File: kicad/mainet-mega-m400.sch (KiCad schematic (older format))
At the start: 4 parts, among them J40 Screw_Terminal_01x04, J64 Screw_Terminal_01x09, J65 Screw_Terminal_01x17, J66 Screw_Terminal_01x02

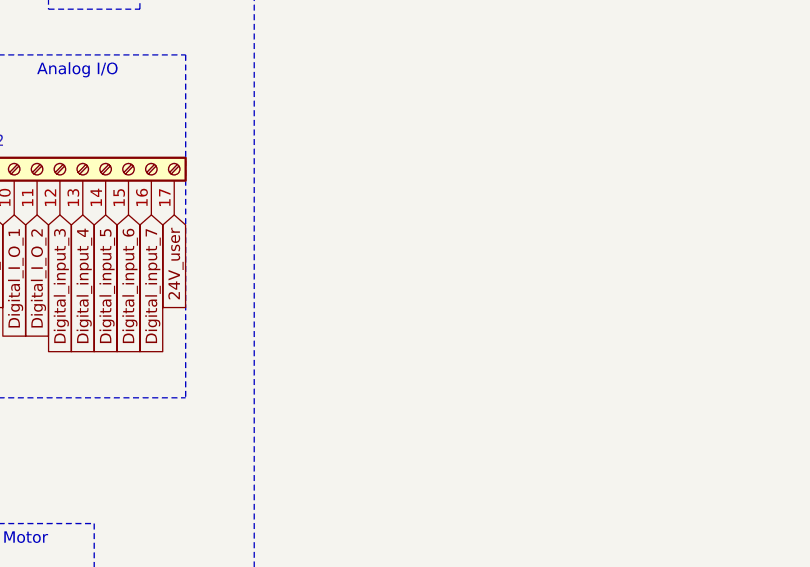
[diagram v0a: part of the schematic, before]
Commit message: KICAD: Actualizar esquemáticos
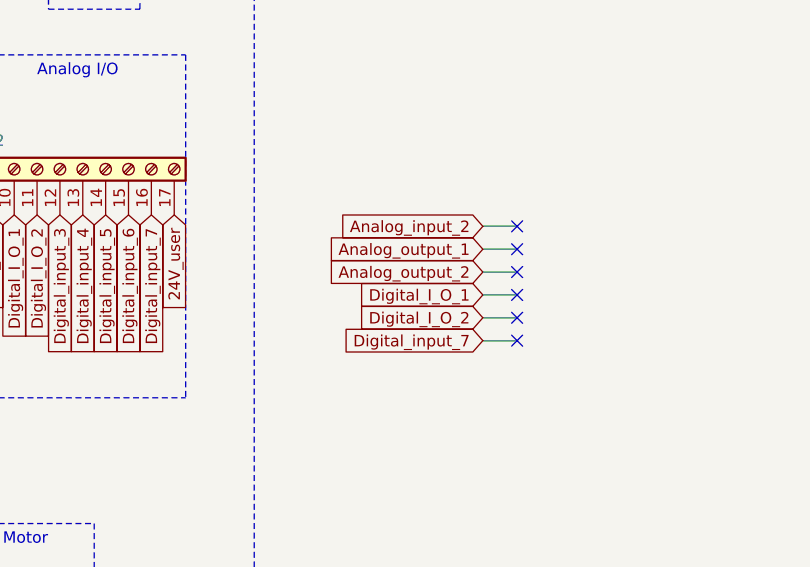
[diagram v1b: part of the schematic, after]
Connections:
- no-connect marks 6 -> 12
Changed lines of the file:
@@
 encoding utf-8
 Sheet 20 21
-Title "Mainet-mega -- "
-Date "2021-04-06"
+Title "Mainet-mega -- Diagrama de Conexiones del M400"
+Date "2021-04-07"
 Rev "1.0"
 Comp "Tovenca"
@@
 W
 NoConn ~ 7450 4450
+NoConn ~ 5800 5150
+NoConn ~ 5800 4950
+NoConn ~ 5800 5050
+NoConn ~ 5800 4850
+NoConn ~ 5800 4750
+NoConn ~ 5800 4650
+Text GLabel 5650 4650 0    50   Input ~ 0
+Analog_input_2
+Wire Wire Line
+	5650 4650 5800 4650
+Text GLabel 5650 4750 0    50   Input ~ 0
+Analog_output_1
+Text GLabel 5650 4850 0    50   Input ~ 0
+Analog_output_2
+Text GLabel 5650 4950 0    50   Input ~ 0
+Digital_I_O_1
+Text GLabel 5650 5050 0    50   Input ~ 0
+Digital_I_O_2
+Text GLabel 5650 5150 0    50   Input ~ 0
+Digital_input_7
+Wire Wire Line
+	5650 4750 5800 4750
+Wire Wire Line
+	5650 4850 5800 4850
+Wire Wire Line
+	5650 4950 5800 4950
+Wire Wire Line
+	5650 5050 5800 5050
+Wire Wire Line
+	5650 5150 5800 5150
 $EndSCHEMATC

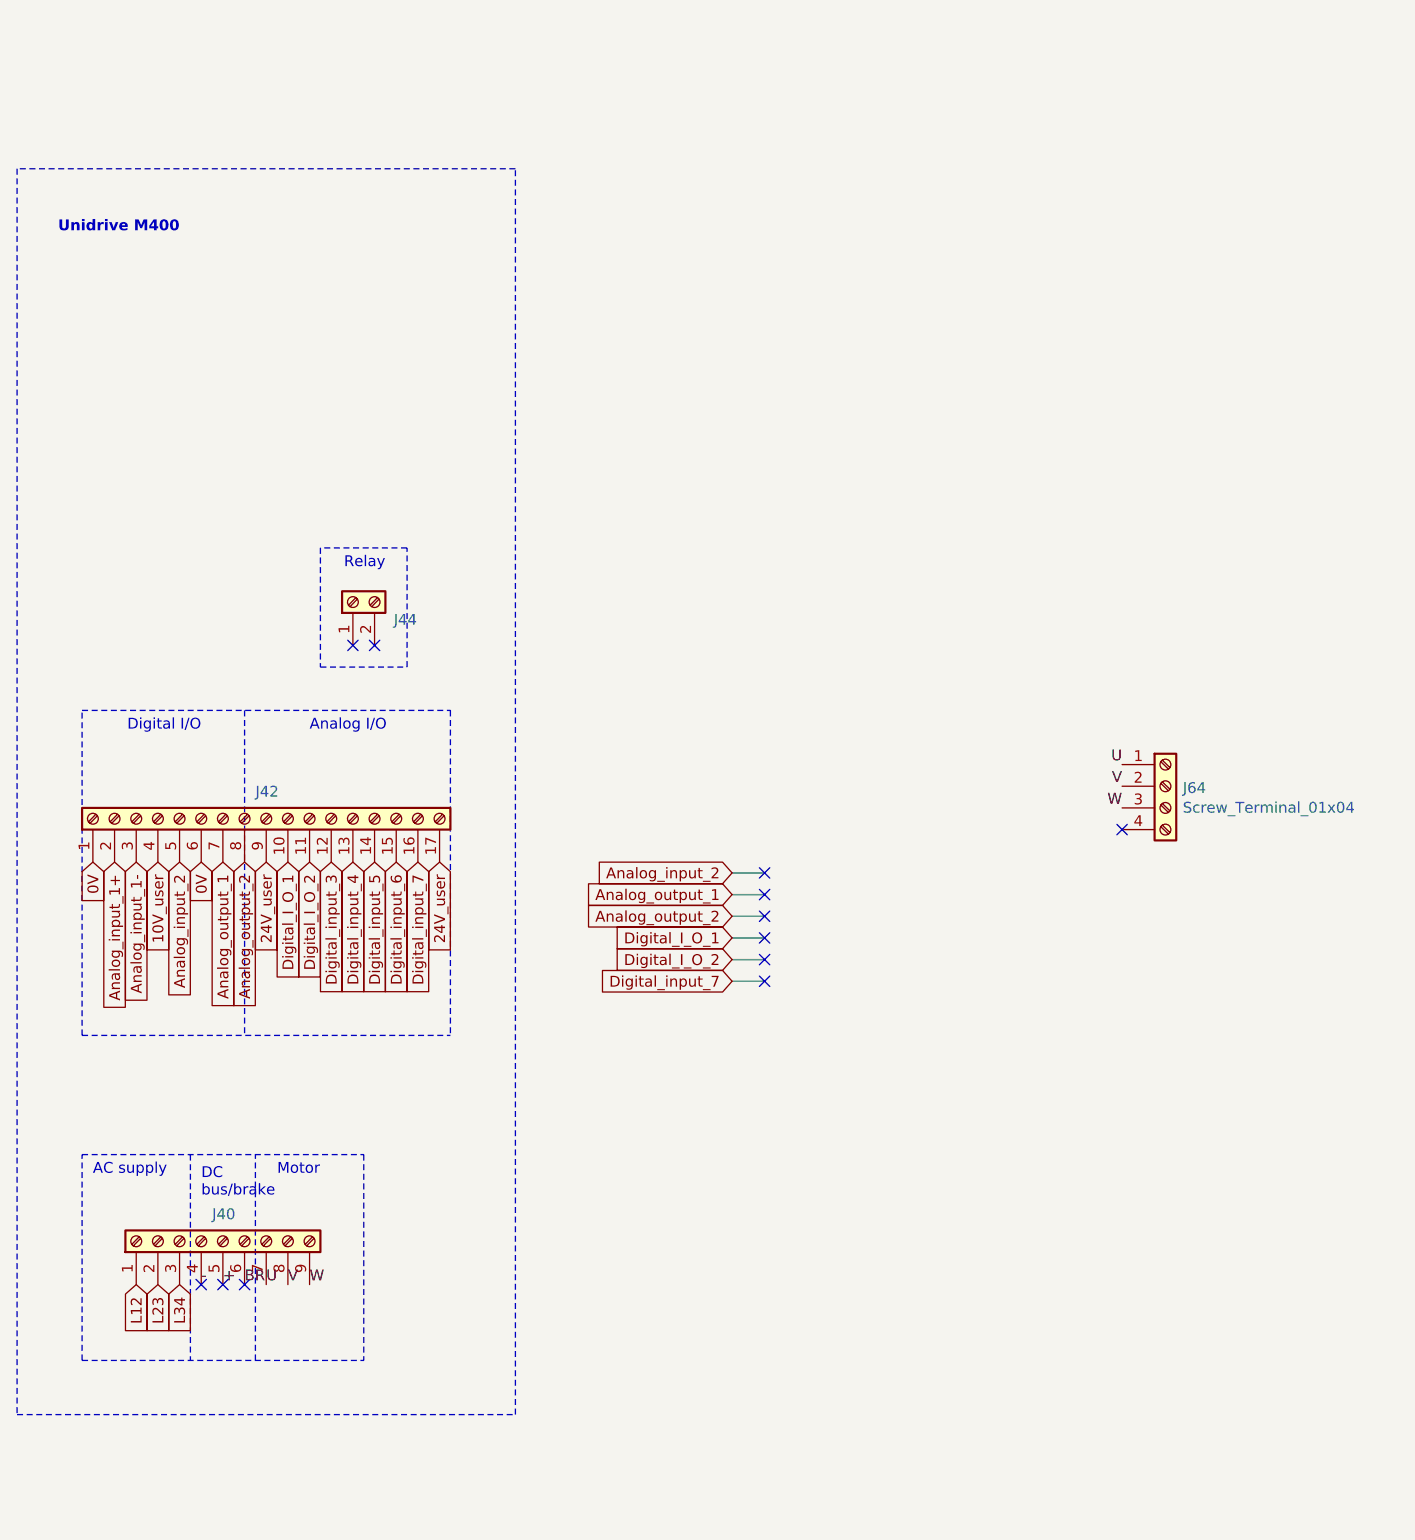
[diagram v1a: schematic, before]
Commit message: KICAD: Corregir kicad/mainet-mega-m400.sch
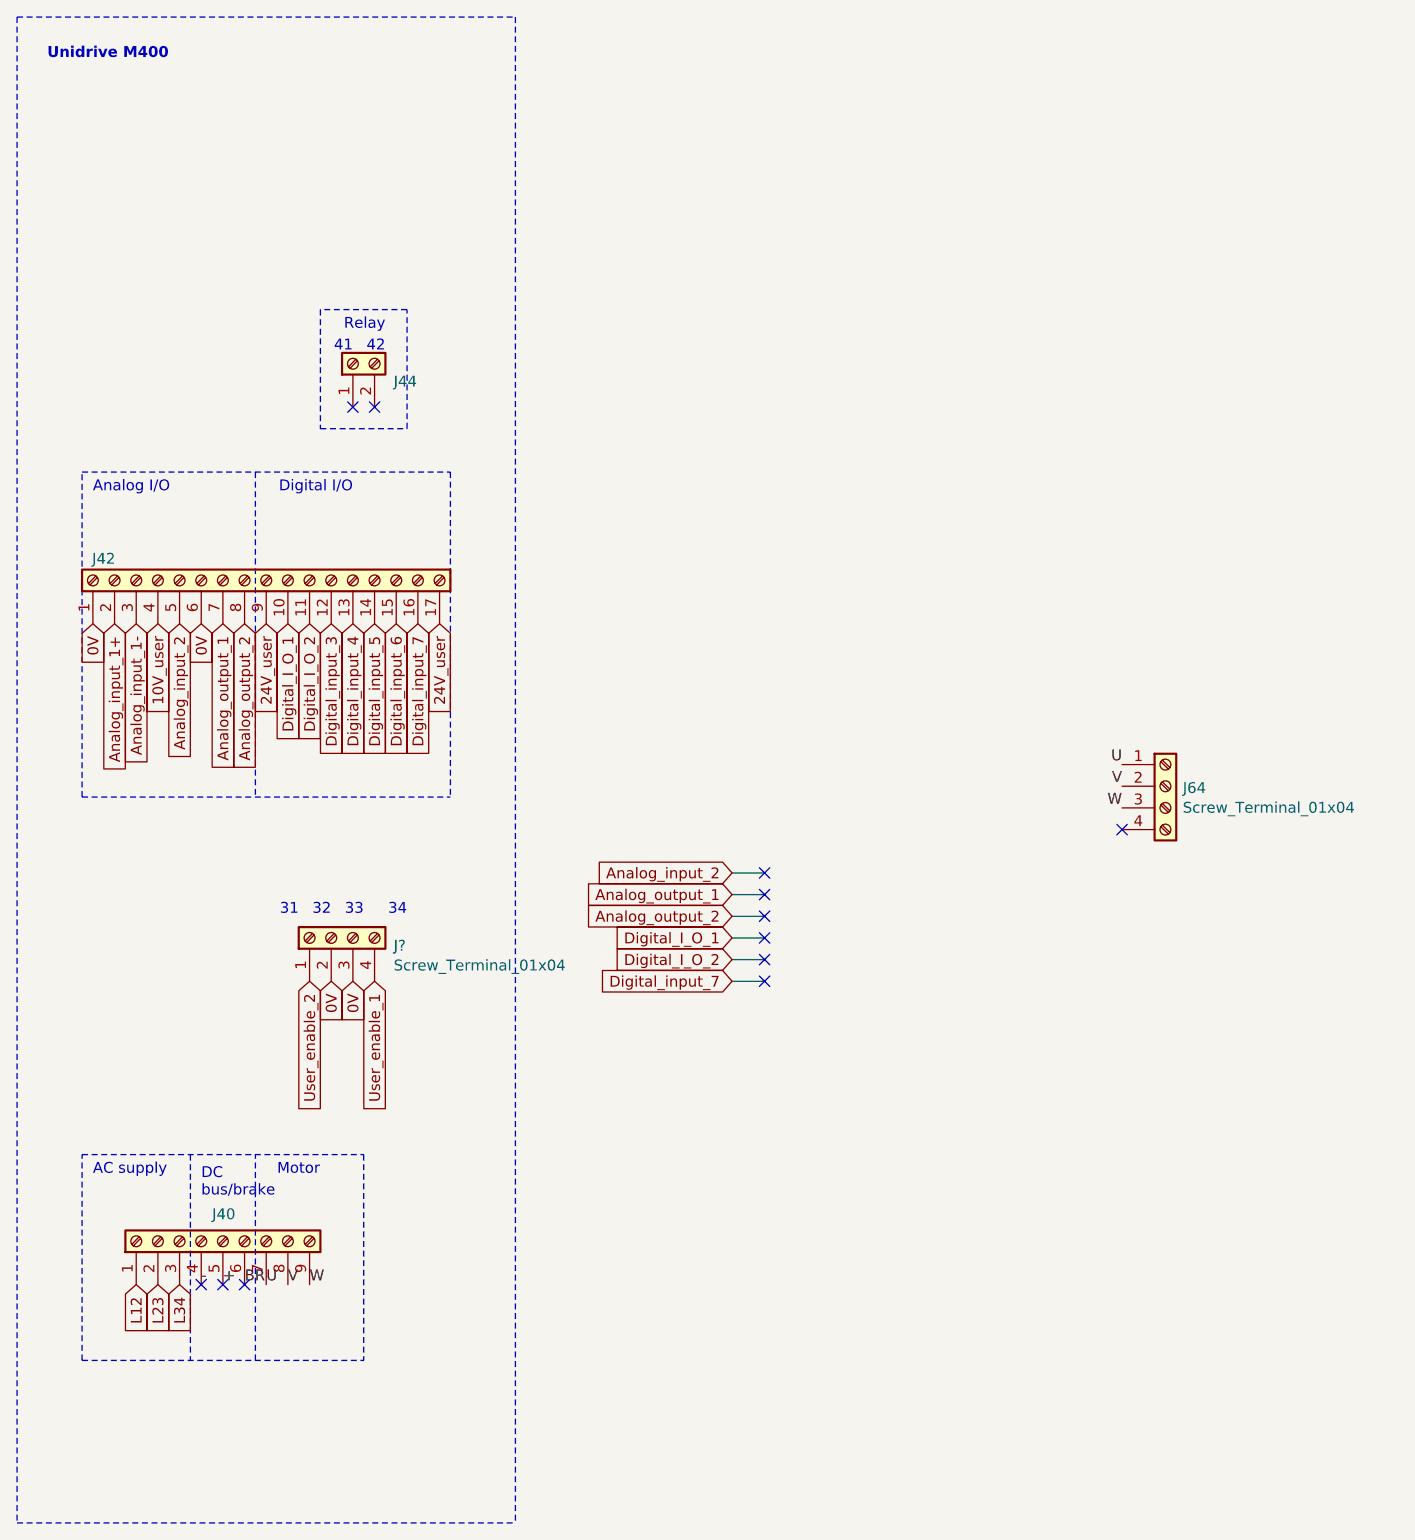
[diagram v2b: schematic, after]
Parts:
- added J?: Screw_Terminal_01x04, symbol Connector:Screw_Terminal_01x04
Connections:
- net 0V: now also J?.2 (Pin_2), J?.3 (Pin_3)
- new net User_enable_1: J?.4 (Pin_4)
- new net User_enable_2: J?.1 (Pin_1)
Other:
- note added: "31"
- note added: "32\n"
- note added: "33"
- note added: "34"
- note added: "41"
- note added: "42"
- moved on the sheet: J42, J44
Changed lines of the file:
@@
 EESchema Schematic File Version 4
+LIBS:mainet-mega-cache
 EELAYER 30 0
 EELAYER END
@@
 Sheet 20 21
 Title "Mainet-mega -- Diagrama de Conexiones del M400"
-Date "2021-04-07"
+Date "2021-06-16"
 Rev "1.0"
 Comp "Tovenca"
@@
 L Connector:Screw_Terminal_01x17 J65
 U 1 1 5FF5E302
-P 3500 4400
+P 3500 3300
 AR Path="/5FC25793/5FF5E17E/5FF5E302" Ref="J65"  Part="1"
 AR Path="/601B5E4D/5FF5E302" Ref="J42"  Part="1"
-F 0 "J42" V 3625 4396 50  0000 C CNN
-F 1 "Screw_Terminal_01x17" H 3580 4351 50  0001 L CNN
-F 2 "" H 3500 4400 50  0001 C CNN
-F 3 "~" H 3500 4400 50  0001 C CNN
-	1    3500 4400
-	0    -1   -1   0
-$EndComp
-Text GLabel 3200 4600 3    50   Input ~ 0
-0V
-Text GLabel 3500 4600 3    50   Input ~ 0
+F 0 "J42" V 3600 4050 50  0000 C CNN
+F 1 "Screw_Terminal_01x17" H 3580 3251 50  0001 L CNN
+F 2 "" H 3500 3300 50  0001 C CNN
+F 3 "~" H 3500 3300 50  0001 C CNN
+	1    3500 3300
+	0    -1   -1   0
+$EndComp
+Text GLabel 3200 3500 3    50   Input ~ 0
+0V
+Text GLabel 3500 3500 3    50   Input ~ 0
 24V_user
-Text GLabel 3600 4600 3    50   Input ~ 0
+Text GLabel 3600 3500 3    50   Input ~ 0
 Digital_I_O_1
-Text GLabel 3700 4600 3    50   Input ~ 0
+Text GLabel 3700 3500 3    50   Input ~ 0
 Digital_I_O_2
-Text GLabel 3800 4600 3    50   Input ~ 0
+Text GLabel 3800 3500 3    50   Input ~ 0
 Digital_input_3
-Text GLabel 3900 4600 3    50   Input ~ 0
+Text GLabel 3900 3500 3    50   Input ~ 0
 Digital_input_4
-Text GLabel 4000 4600 3    50   Input ~ 0
+Text GLabel 4000 3500 3    50   Input ~ 0
 Digital_input_5
-Text GLabel 4100 4600 3    50   Input ~ 0
+Text GLabel 4100 3500 3    50   Input ~ 0
 Digital_input_6
-Text GLabel 4200 4600 3    50   Input ~ 0
+Text GLabel 4200 3500 3    50   Input ~ 0
 Digital_input_7
-Text GLabel 4300 4600 3    50   Input ~ 0
+Text GLabel 4300 3500 3    50   Input ~ 0
 24V_user
-Text GLabel 2700 4600 3    50   Input ~ 0
-0V
-Text GLabel 2800 4600 3    50   Input ~ 0
+Text GLabel 2700 3500 3    50   Input ~ 0
+0V
+Text GLabel 2800 3500 3    50   Input ~ 0
 Analog_input_1+
-Text GLabel 2900 4600 3    50   Input ~ 0
+Text GLabel 2900 3500 3    50   Input ~ 0
 Analog_input_1-
-Text GLabel 3000 4600 3    50   Input ~ 0
+Text GLabel 3000 3500 3    50   Input ~ 0
 10V_user
-Text GLabel 3100 4600 3    50   Input ~ 0
+Text GLabel 3100 3500 3    50   Input ~ 0
 Analog_input_2
-Text GLabel 3300 4600 3    50   Input ~ 0
+Text GLabel 3300 3500 3    50   Input ~ 0
 Analog_output_1
-Text GLabel 3400 4600 3    50   Input ~ 0
+Text GLabel 3400 3500 3    50   Input ~ 0
 Analog_output_2
 $Comp
 L Connector:Screw_Terminal_01x02 J66
 U 1 1 5FF6D0E6
-P 3900 3400
+P 3900 2300
 AR Path="/5FC25793/5FF5E17E/5FF6D0E6" Ref="J66"  Part="1"
 AR Path="/601B5E4D/5FF6D0E6" Ref="J44"  Part="1"
-F 0 "J44" V 3818 3212 50  0000 R CNN
-F 1 "Screw_Terminal_01x02" V 3773 3212 50  0001 R CNN
-F 2 "" H 3900 3400 50  0001 C CNN
-F 3 "~" H 3900 3400 50  0001 C CNN
-	1    3900 3400
+F 0 "J44" V 3818 2112 50  0000 R CNN
+F 1 "Screw_Terminal_01x02" V 3773 2112 50  0001 R CNN
+F 2 "" H 3900 2300 50  0001 C CNN
+F 3 "~" H 3900 2300 50  0001 C CNN
+	1    3900 2300
 	0    -1   -1   0
 $EndComp
@@
 DC\nbus/brake\n
 Wire Notes Line
-	3400 3900 3400 5400
-Wire Notes Line
-	2650 5400 2650 3900
-Wire Notes Line
-	4350 3900 4350 5400
-Wire Notes Line
-	2650 5400 4350 5400
-Wire Notes Line
-	2650 3900 4350 3900
-Text Notes 3700 4000 0    50   ~ 0
+	2650 4300 2650 2800
+Wire Notes Line
+	4350 2800 4350 4300
+Wire Notes Line
+	2650 4300 4350 4300
+Wire Notes Line
+	2650 2800 4350 2800
+Text Notes 2700 2900 0    50   ~ 0
 Analog I/O
-Text Notes 3200 4000 2    50   ~ 0
+Text Notes 3900 2900 2    50   ~ 0
 Digital I/O
 Wire Notes Line
-	3750 3700 4150 3700
-Wire Notes Line
-	4150 3700 4150 3150
-Wire Notes Line
-	4150 3150 3750 3150
-Wire Notes Line
-	3750 3150 3750 3700
-Text Notes 4050 3250 2    50   ~ 0
+	3750 2600 4150 2600
+Wire Notes Line
+	4150 2600 4150 2050
+Wire Notes Line
+	4150 2050 3750 2050
+Wire Notes Line
+	3750 2050 3750 2600
+Text Notes 4050 2150 2    50   ~ 0
 Relay
-Wire Notes Line
-	2350 7150 4650 7150
-Wire Notes Line
-	4650 7150 4650 1400
-Wire Notes Line
-	4650 1400 2350 1400
-Wire Notes Line
-	2350 1400 2350 7150
-Text Notes 3100 1700 2    50   ~ 10
+Text Notes 3050 900  2    50   ~ 10
 Unidrive M400
-NoConn ~ 3900 3600
-NoConn ~ 4000 3600
+NoConn ~ 3900 2500
+NoConn ~ 4000 2500
 NoConn ~ 3200 6550
 NoConn ~ 3300 6550
@@
 Wire Wire Line
 	5650 5150 5800 5150
+Wire Notes Line
+	2350 7650 4650 7650
+Wire Notes Line
+	2350 700  4650 700
+Wire Notes Line
+	2350 700  2350 7650
+Wire Notes Line
+	4650 700  4650 7650
+$Comp
+L Connector:Screw_Terminal_01x04 J?
+U 1 1 60CBF2D5
+P 3800 4950
+F 0 "J?" V 3764 4662 50  0000 R CNN
+F 1 "Screw_Terminal_01x04" V 3673 4662 50  0000 R CNN
+F 2 "" H 3800 4950 50  0001 C CNN
+F 3 "~" H 3800 4950 50  0001 C CNN
+	1    3800 4950
+	0    -1   -1   0
+$EndComp
+Text GLabel 3700 5150 3    50   Input ~ 0
+User_enable_2
+Text GLabel 4000 5150 3    50   Input ~ 0
+User_enable_1
+Text GLabel 3800 5150 3    50   Input ~ 0
+0V
+Text GLabel 3900 5150 3    50   Input ~ 0
+0V
+Wire Notes Line
+	3450 2800 3450 4300
+Text Notes 3650 4850 2    50   ~ 0
+31
+Text Notes 3800 4850 2    50   ~ 0
+32\n
+Text Notes 3950 4850 2    50   ~ 0
+33
+Text Notes 4150 4850 2    50   ~ 0
+34
+Text Notes 3900 2250 2    50   ~ 0
+41
+Text Notes 4050 2250 2    50   ~ 0
+42
 $EndSCHEMATC

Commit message: KICAD: Modificar esquemático m400
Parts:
- gave numbers to parts that had none: 1
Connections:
- net User_enable_1: no longer names the net of J88.4 (Pin_4)
- no-connect marks 12 -> 13
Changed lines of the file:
@@
 	4650 700  4650 7650
 $Comp
-L Connector:Screw_Terminal_01x04 J?
+L Connector:Screw_Terminal_01x04 J88
 U 1 1 60CBF2D5
 P 3800 4950
-F 0 "J?" V 3764 4662 50  0000 R CNN
+F 0 "J88" V 3764 4662 50  0000 R CNN
 F 1 "Screw_Terminal_01x04" V 3673 4662 50  0000 R CNN
 F 2 "" H 3800 4950 50  0001 C CNN
@@
 Text GLabel 3700 5150 3    50   Input ~ 0
 User_enable_2
-Text GLabel 4000 5150 3    50   Input ~ 0
-User_enable_1
 Text GLabel 3800 5150 3    50   Input ~ 0
 0V
@@
 Text Notes 4050 2250 2    50   ~ 0
 42
+NoConn ~ 4000 5150
 $EndSCHEMATC
